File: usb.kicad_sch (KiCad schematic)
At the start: 9 parts, among them J4 USB, U2 FT230XS

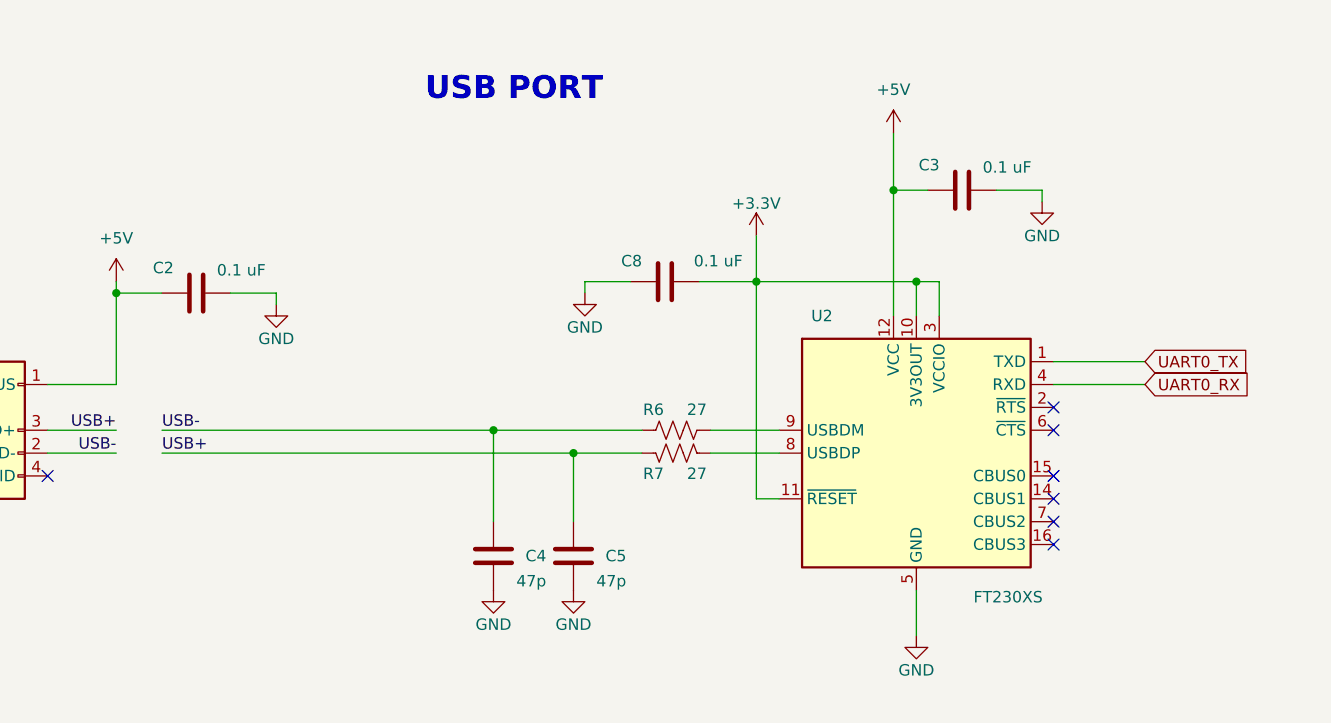
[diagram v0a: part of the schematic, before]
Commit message: major finishing touches:     - major rework for v5.1     - silkscreen and stuff     - impednace for USB and CAN lines     - schematic comments     - symbol, footprint, and model library updates
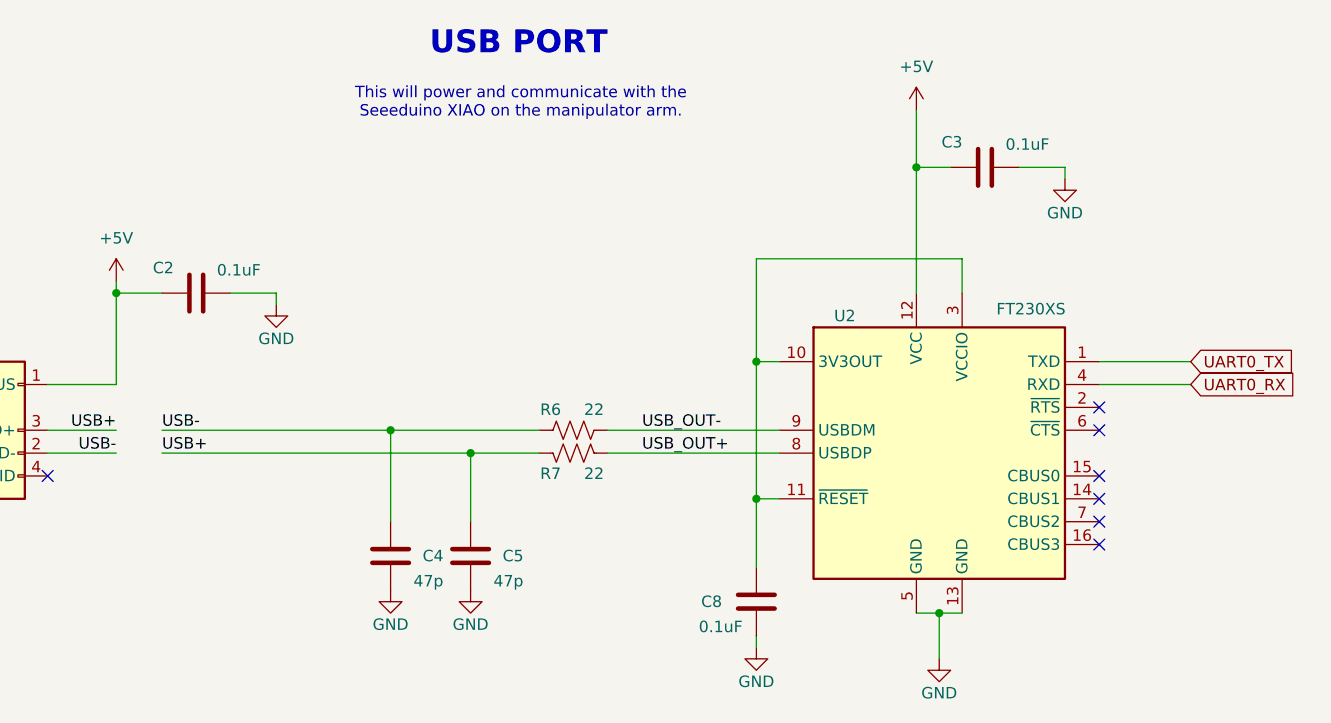
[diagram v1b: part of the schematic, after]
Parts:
- C2, C3, C8: value 0.1 uF -> 0.1uF; Manufacturer (none) -> KEMET; Manufacturer Part Number (none) -> C1206C104J5RACTU; Vendor (none) -> Digikey; Vendor Part Number (none) -> 399-C1206C104J5RACTUCT-ND
- C4, C5: Manufacturer (none) -> KEMET; Manufacturer Part Number (none) -> C0603C470K5RACTU; Vendor (none) -> Digikey; Vendor Part Number (none) -> 399-C0603C470K5RACTUCT-ND
- J4: Manufacturer (none) -> Würth Elektronik; Manufacturer Part Number (none) -> 629105150521; Vendor (none) -> Digikey; Vendor Part Number (none) -> 732-5960-1-ND
- R6, R7: value 27 -> 22; Manufacturer (none) -> Stackpole Electronics Inc; Manufacturer Part Number (none) -> RNCP0603FTD22R1; Vendor (none) -> Digikey; Vendor Part Number (none) -> RNCP0603FTD22R1CT-ND
- U2: footprint Package_SO:SSOP-20_3.9x8.7mm_P0.635mm -> Package_SO:SSOP-16_3.9x4.9mm_P0.635mm; Manufacturer (none) -> FTDI, Future Technology Devices International Ltd; Manufacturer Part Number (none) -> FT230XS-R; Vendor (none) -> Digikey; Vendor Part Number (none) -> 768-1135-1-ND
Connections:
- net USB_OUT-: now reaches R6.2, U2.9 (USBDM)
- net USB_OUT+: now reaches R7.2, U2.8 (USBDP)
- net +3.3V: no longer names the net of C8.2, U2.10 (3V3OUT), U2.11 (~{RESET}), U2.3 (VCCIO)
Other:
- note added: "This will power and communicate with the Seeeduino XIAO on the manipulator arm."
- company: WVU Unviersity Rover Challenge -> WVU Unviersity Rover Challenge (URC)
- moved on the sheet: C3, C4, C5, C8, R6, R7

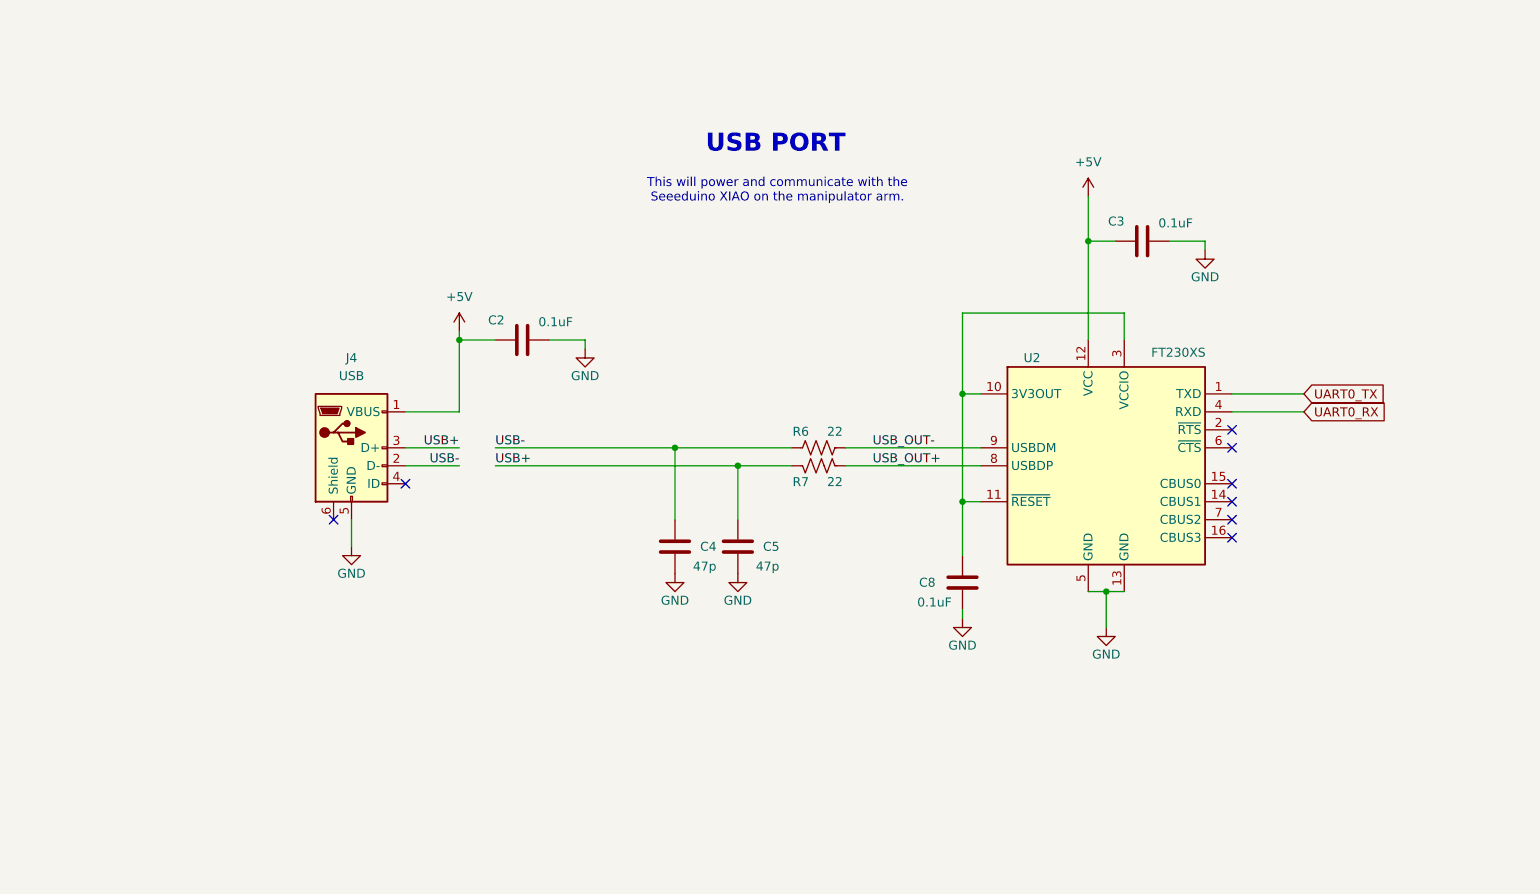
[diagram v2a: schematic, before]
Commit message: swapped UART to USB from FTDI (out of stock) to MCP2200
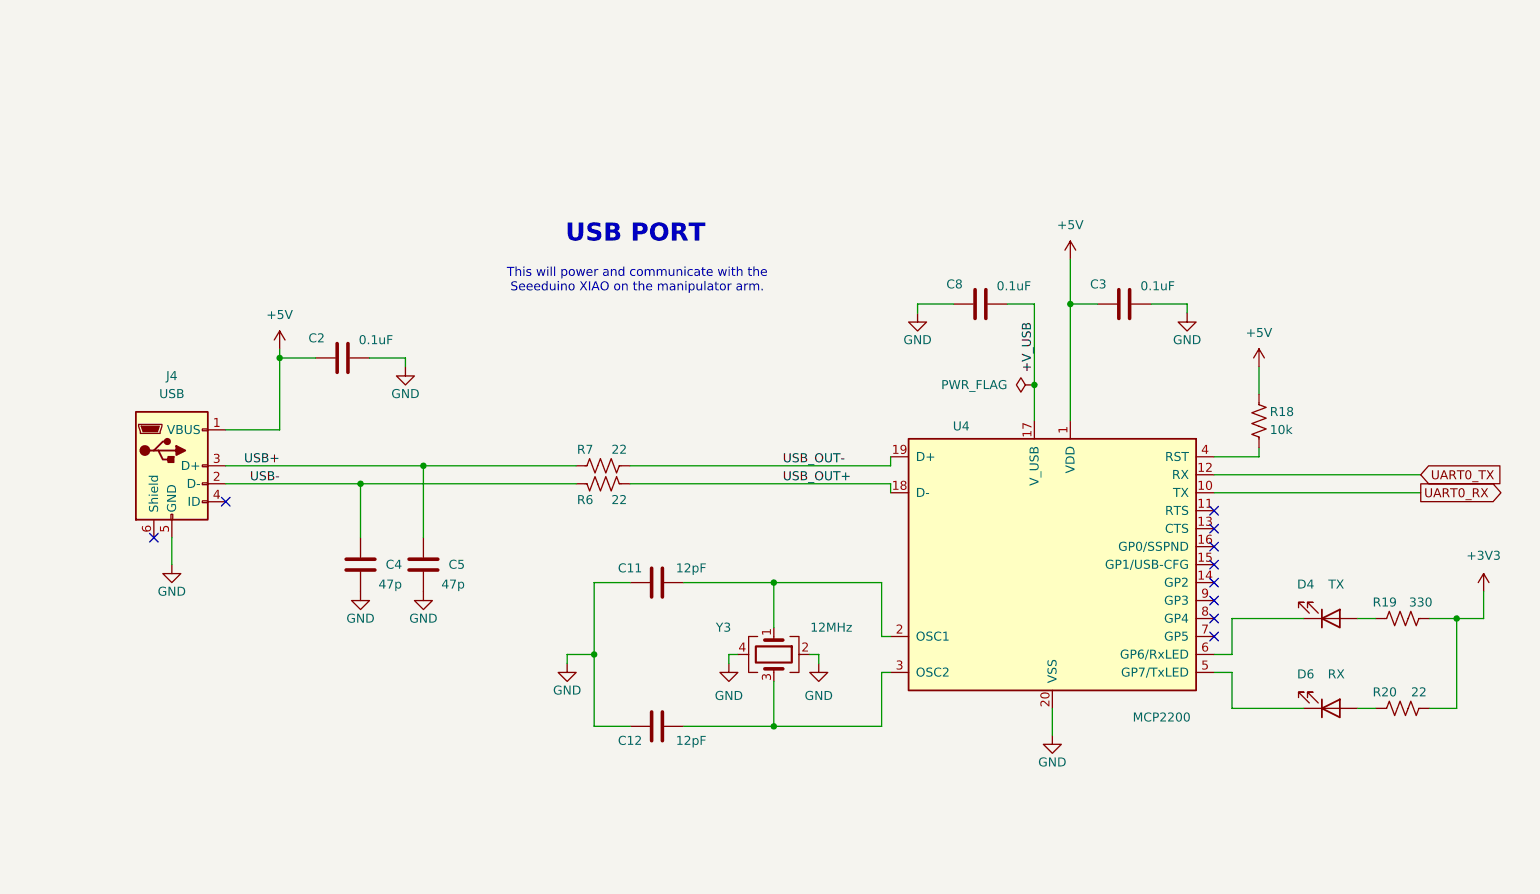
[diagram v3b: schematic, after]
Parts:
- removed U2: FT230XS, Package_SO:SSOP-16_3.9x4.9mm_P0.635mm, symbol Interface_USB:FT230XS
- added C11, C12: 12pF, Capacitor_SMD:C_0603_1608Metric_Pad1.08x0.95mm_HandSolder, symbol Device:C
- added D4: TX, LED_SMD:LED_0805_2012Metric_Pad1.15x1.40mm_HandSolder, symbol Device:LED
- added D6: RX, LED_SMD:LED_0805_2012Metric_Pad1.15x1.40mm_HandSolder, symbol Device:LED
- added R18: 10k, Resistor_SMD:R_0603_1608Metric_Pad0.98x0.95mm_HandSolder, symbol Device:R_US
- added R19: 330, Resistor_SMD:R_0603_1608Metric_Pad0.98x0.95mm_HandSolder, symbol Device:R_US
- added R20: 22, Resistor_SMD:R_0603_1608Metric_Pad0.98x0.95mm_HandSolder, symbol Device:R_US
- added U4: MCP2200, Package_SO:SSOP-20_5.3x7.2mm_P0.65mm, symbol Interface_USB:MCP2200T-E-SS
- added Y3: 12MHz, Crystal:Crystal_SMD_2520-4Pin_2.5x2.0mm, symbol Device:Crystal_GND24
- C2, C3, C8: footprint Capacitor_SMD:C_1206_3216Metric_Pad1.33x1.80mm_HandSolder -> Capacitor_SMD:C_0805_2012Metric_Pad1.18x1.45mm_HandSolder
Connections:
- net +5V: now also R18.2, U4.1 (VDD)
- net GND: now also C8.2, C11.1, C12.1, U4.20 (VSS), Y3.2, Y3.4; no longer C8.1
- net UART0_RX: now also U4.10 (TX)
- net UART0_TX: now also U4.12 (RX)
- net USB_OUT+: now also R6.2, U4.18 (D-); no longer R7.2
- net USB_OUT-: now also R7.2, U4.19 (D+); no longer R6.2
- new net: D4.2 (A), R19.2
- new net: D6.1 (K), U4.5 (GP7/TxLED)
- new net: D6.2 (A), R20.1
- new net: D4.1 (K), U4.6 (GP6/RxLED)
- new net: C11.2, U4.2 (OSC1), Y3.1
- new net: C12.2, U4.3 (OSC2), Y3.3
- new net: R18.1, U4.4 (RST)
- new net +3V3: R19.1, R20.2
- new net +V_USB: C8.1, U4.17 (V_USB)
- no-connect marks 8 -> 10
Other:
- moved on the sheet: C2, C3, C4, C5, J4, R6, R7

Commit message: added release documents for v5.1 (pending approval)
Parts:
- J4: Manufacturer Würth Elektronik -> Wurth Elektronik
- renumbered Y3 to Y2
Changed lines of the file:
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@@
 			)
 		)
-		(property "Manufacturer" "Würth Elektronik"
+		(property "Manufacturer" "Wurth Elektronik"
 			(at 60.96 95.25 0)
 			(effects
@@
 		(on_board yes)
 		(dnp no)
-		(property "Reference" "Y3"
+		(property "Reference" "Y2"
 			(at 138.938 118.11 90)
 			(effects
@@
 			(project ""
 				(path "/29e78086-2175-405e-9ba3-c48766d2f50c/ed009bc9-eb74-4cea-8f66-c2275b048d81"
-					(reference "Y3")
-					(unit 1)
-				)
+					(reference "Y2")
+					(unit 1)
+				)

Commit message: touch ups from peer reviews
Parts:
- added C16: 0.1uF, Capacitor_SMD:C_0805_2012Metric_Pad1.18x1.45mm_HandSolder, symbol Device:C
- added U2: MIC94093YC6, Package_TO_SOT_SMD:SOT-363_SC-70-6, symbol Power_Management:MIC94093YC6
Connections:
- net +5V: now also C16.2, U2.4 (IN), U2.6 (EN); no longer C2.2, J4.1 (VBUS)
- net GND: now also C16.1, U2.2 (GND), U2.5 (GND)
- net USB_OUT+: now also R7.2, U4.19 (D+); no longer R6.2, U4.18 (D-)
- net USB_OUT-: now also R6.2, U4.18 (D-); no longer R7.2, U4.19 (D+)
- new net +VBUS: C2.2, J4.1 (VBUS), U2.1 (OUT)
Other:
- note added: "High-side load switch with soft start. 1.2A continuous, 790us soft start, auto-discharge."
- note added: "SOFT START SWITCH"
- note added: "UART TO USB"
- note added: "USB 2.0 to UART Converter by Microchip"
- moved on the sheet: C11, C12, C2, C3, C4, C5, C8, D4, D6, J4, R18, R19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

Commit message: Added housing/cable/header info to each connector's symbol properties.
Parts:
- J4: Cable (none) -> U040-006-MICRO
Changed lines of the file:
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@@
 			)
 		)
+		(property "Housing" ""
+			(at 236.22 132.08 90)
+			(effects
+				(font
+					(size 1.27 1.27)
+				)
+				(hide yes)
+			)
+		)
 		(pin "1"
 		)
@@
 			)
 		)
+		(property "Cable" "U040-006-MICRO"
+			(at 62.23 110.49 0)
+			(effects
+				(font
+					(size 1.27 1.27)
+				)
+				(hide yes)
+			)
+		)
+		(property "Housing" ""
+			(at 62.23 110.49 0)
+			(effects
+				(font
+					(size 1.27 1.27)
+				)
+				(hide yes)
+			)
+		)
 		(pin "2"
 		)
@@
 			)
 		)
+		(property "Housing" ""
+			(at 226.06 144.78 0)
+			(effects
+				(font
+					(size 1.27 1.27)
+				)
+				(hide yes)
+			)
+		)
 		(pin "1"
 		)
@@
 			)
 		)
+		(property "Housing" ""
+			(at 176.53 87.63 90)
+			(effects
+				(font
+					(size 1.27 1.27)
+				)
+				(hide yes)
+			)
+		)
 		(pin "1"
 		)
@@
 			)
 		)
+		(property "Housing" ""
+			(at 123.19 113.03 90)
+			(effects
+				(font
+					(size 1.27 1.27)
+				)
+				(hide yes)
+			)
+		)
 		(pin "2"
 		)
@@
 			)
 		)
+		(property "Housing" ""
+			(at 226.06 132.08 0)
+			(effects
+				(font
+					(size 1.27 1.27)
+				)
+				(hide yes)
+			)
+		)
 		(pin "1"
 		)
@@
 			)
 		)
+		(property "Housing" ""
+			(at 88.9 124.46 0)
+			(effects
+				(font
+					(size 1.27 1.27)
+				)
+				(hide yes)
+			)
+		)
 		(pin "1"
 		)
@@
 			)
 		)
+		(property "Housing" ""
+			(at 186.69 124.46 0)
+			(effects
+				(font
+					(size 1.27 1.27)
+				)
+				(hide yes)
+			)
+		)
 		(pin "17"
 		)
@@
 			)
 		)
+		(property "Housing" ""
+			(at 97.79 124.46 0)
+			(effects
+				(font
+					(size 1.27 1.27)
+				)
+				(hide yes)
+			)
+		)
 		(pin "1"
 		)
@@
 			)
 		)
+		(property "Housing" ""
+			(at 130.81 127 90)
+			(effects
+				(font
+					(size 1.27 1.27)
+				)
+				(hide yes)
+			)
+		)
 		(pin "1"
 		)
@@
 			)
 		)
+		(property "Housing" ""
+			(at 72.39 60.96 90)
+			(effects
+				(font
+					(size 1.27 1.27)
+				)
+				(hide yes)
+			)
+		)
 		(pin "1"
 		)
@@
 			)
 		)
+		(property "Housing" ""
+			(at 147.32 137.16 90)
+			(effects
+				(font
+					(size 1.27 1.27)
+				)
+				(hide yes)
+			)
+		)
 		(pin "2"
 		)
@@
 			)
 		)
+		(property "Housing" ""
+			(at 95.25 63.5 0)
+			(effects
+				(font
+					(size 1.27 1.27)
+				)
+				(hide yes)
+			)
+		)
 		(pin "2"
 		)
@@
 			)
 		)
+		(property "Housing" ""
+			(at 123.19 110.49 90)
+			(effects
+				(font
+					(size 1.27 1.27)
+				)
+				(hide yes)
+			)
+		)
 		(pin "2"
 		)
@@
 			)
 		)
+		(property "Housing" ""
+			(at 118.11 60.96 90)
+			(effects
+				(font
+					(size 1.27 1.27)
+				)
+				(hide yes)
+			)
+		)
 		(pin "1"
 		)
@@
 			)
 		)
+		(property "Housing" ""
+			(at 215.9 104.14 0)
+			(effects
+				(font
+					(size 1.27 1.27)
+				)
+				(hide yes)
+			)
+		)
 		(pin "1"
 		)
@@
 			)
 		)
+		(property "Housing" ""
+			(at 130.81 147.32 90)
+			(effects
+				(font
+					(size 1.27 1.27)
+				)
+				(hide yes)
+			)
+		)
 		(pin "1"
 		)
@@
 			)
 		)
+		(property "Housing" ""
+			(at 236.22 144.78 90)
+			(effects
+				(font
+					(size 1.27 1.27)
+				)
+				(hide yes)
+			)
+		)
 		(pin "2"
 		)
@@
 			(effects
 				(font
+					(size 1.27 1.27)
+				)
+				(hide yes)
+			)
+		)
+		(property "Housing" ""
+			(at 196.85 87.63 90)
+			(effects
+				(font
